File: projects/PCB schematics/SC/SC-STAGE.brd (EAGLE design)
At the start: 160 x 100 mm, 0 parts

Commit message: SC - Stage initial placement.
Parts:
- added BSPD, BSPDPLAUS1, BSPDPLAUS2, IMD: (no value), con-lstb:MA03-1
- added LED1, LED2, LED3, LED4: 150080VS75000, 150080VS75000:LEDC2012X80N
- added NOT1: 74LS19D, 74xx-us:SO14
- added Q1, Q2, Q3, Q4: IRLZ44Z, transistor-power:TO220BH
- added R1, R10, R11, R12, R2, R3, R4, R9: (no value), rcl:R0805
- added R13, R14, R5, R6: 47k, rcl:R0805
- added R15, R16, R7, R8: 100, rcl:R0805
- added U1, U2, U3, U4: G5LE-1A-E-DC12, IowaFormula:G5LE-1A-E-DC12
- added X1, X3, X4, X5, X6: 5566-2, con-molex:5566-2
- added X2: 5566-4, con-molex:5566-4
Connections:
- new net +12V: U1.5, U2.5, U3.5, U4.5
- new net +12V-ISO: X1.1, X1.2
- new net BSPDFAULT_LED: BSPD.1, X2.1
- new net BSPDPLAUS1_LED: BSPDPLAUS1.1, X2.2
- new net BSPDPLAUS2_LED: BSPDPLAUS2.1, X2.3
- new net GND: BSPD.3, BSPDPLAUS1.3, BSPDPLAUS2.3, IMD.3, NOT1.7, Q1.S, Q2.S, Q3.S, Q4.S, R11.1, R12.1, R13.1, R14.1, R3.1, R4.1, R5.1, R6.1, X5.1, X5.2
- new net IMDFAULT_LED: IMD.1, X2.4
- new net LED4: LED4.1, R11.2
- new net N$1: Q1.G, R7.2
- new net N$10: U3.1, U4.3
- new net N$105105: BSPD.2, NOT1.13, R1.1
- new net N$11552: BSPDPLAUS1.2, NOT1.11, R2.1
- new net N$14: Q4.G, R15.2
- new net N$15: LED4.2, NOT1.2, R13.2, R15.1
- new net N$17: Q4.D, U4.2
- new net N$18: Q3.G, R16.2
- new net N$19: LED3.2, NOT1.8, R14.2, R16.1
- new net N$2: LED1.2, NOT1.12, R5.2, R7.1
- new net N$20: LED3.1, R12.2
- new net N$21: Q3.D, U3.2
- new net N$3: LED1.1, R3.2
- new net N$38: U2.1, U3.3
- new net N$4: Q1.D, U1.2
- new net N$5: Q2.G, R8.2
- new net N$6: LED2.2, NOT1.10, R6.2, R8.1
- new net N$626: BSPDPLAUS2.2, NOT1.9, R10.1
- new net N$7: LED2.1, R4.2
- new net N$8: Q2.D, U2.2
- new net N$9: U1.1, U2.3
- new net N$9581: IMD.2, NOT1.1, R9.1
- new net SC+: U1.3, X4.1, X4.2
- new net SC-: U4.1, X6.1, X6.2
- new net VCC: NOT1.14, R1.2, R10.2, R2.2, R9.2, X3.1, X3.2
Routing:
- net VCC: track 0.00 -> 93.8 mm, vias 0 -> 5
- net BSPDFAULT_LED: track 0.00 -> 59.4 mm
- net BSPDPLAUS1_LED: track 0.00 -> 38.7 mm
- net BSPDPLAUS2_LED: track 0.00 -> 37.0 mm
- net IMDFAULT_LED: track 0.00 -> 18.1 mm
- net N$105105: track 0.00 -> 18.1 mm
- net N$626: track 0.00 -> 3.94 mm
- net N$11552: track 0.00 -> 3.94 mm
- net N$9581: track 0.00 -> 3.94 mm
- added copper zone on layer 1, net GND
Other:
- board size 160 x 100 mm -> 99.1 x 99.1 mm

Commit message: SC - SC-STAGE Rev. A
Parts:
- moved BSPDPLAUS1 1.27 mm to (53.3, 73.7)
- moved Q1 1.27 mm to (14.0, 55.9)
- moved Q2 1.27 mm to (38.1, 55.9)
- moved Q3 1.27 mm to (61.0, 55.9)
- moved Q4 1.27 mm to (86.4, 55.9)
- moved R2 1.27 mm to (49.5, 74.9)
- renumbered X1 to 12V-ISO, X3 to VCC, X4 to SC+, X5 to GND, X6 to SC-
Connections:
- removed net +12V: U1.5, U2.5, U3.5, U4.5
- net +12V-ISO: now also U1.5, U2.5, U3.5, U4.5
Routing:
- net +12V-ISO: track 0.00 -> 197.2 mm, vias 0 -> 1
- net SC-: track 0.00 -> 157.4 mm
- net N$15: track 0.00 -> 108.1 mm, vias 0 -> 2
- net SC+: track 0.00 -> 104.2 mm
- net N$9581: track 3.94 -> 71.4 mm, vias 0 -> 1
- net N$19: track 0.00 -> 61.9 mm
- net N$6: track 0.00 -> 54.8 mm
- net N$2: track 0.00 -> 53.3 mm, vias 0 -> 2
- net N$626: track 3.94 -> 51.8 mm, vias 0 -> 1
- net N$17: track 0.00 -> 37.1 mm
- net N$8: track 0.00 -> 36.7 mm
- net N$21: track 0.00 -> 36.7 mm
- net N$4: track 0.00 -> 36.6 mm
- net N$11552: track 3.94 -> 37.2 mm, vias 0 -> 1
- net N$14: track 0.00 -> 33.2 mm
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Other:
- board text added: "Authors: github.com/michaelpass"
- board text added: "Iowa Formula"
- board text added: "Off"
- board text added: "On"
- board text added: "Shutdown Fault Staging Board (SC-STAGE) Rev A: May 2nd, 2019"

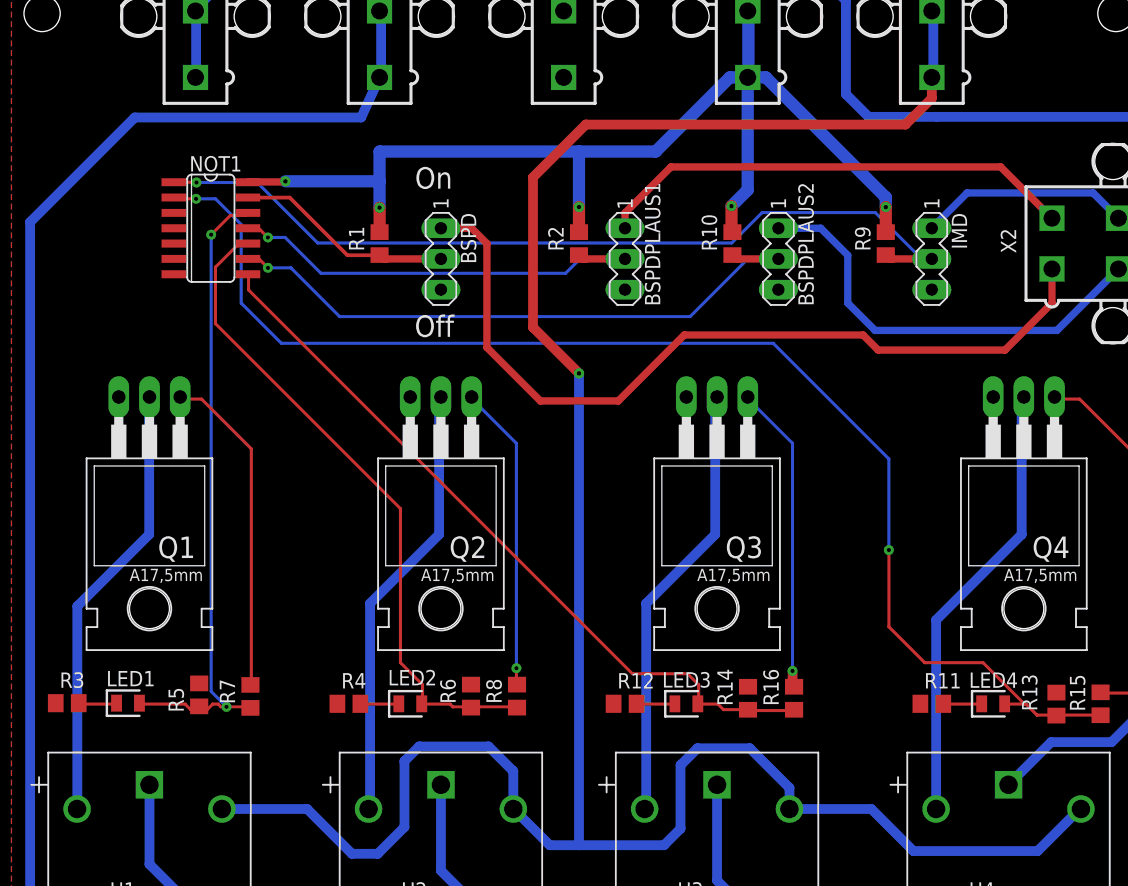
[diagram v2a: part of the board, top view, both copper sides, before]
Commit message: RTDS + TSAL Board update
Minor board & schematic errors corrected
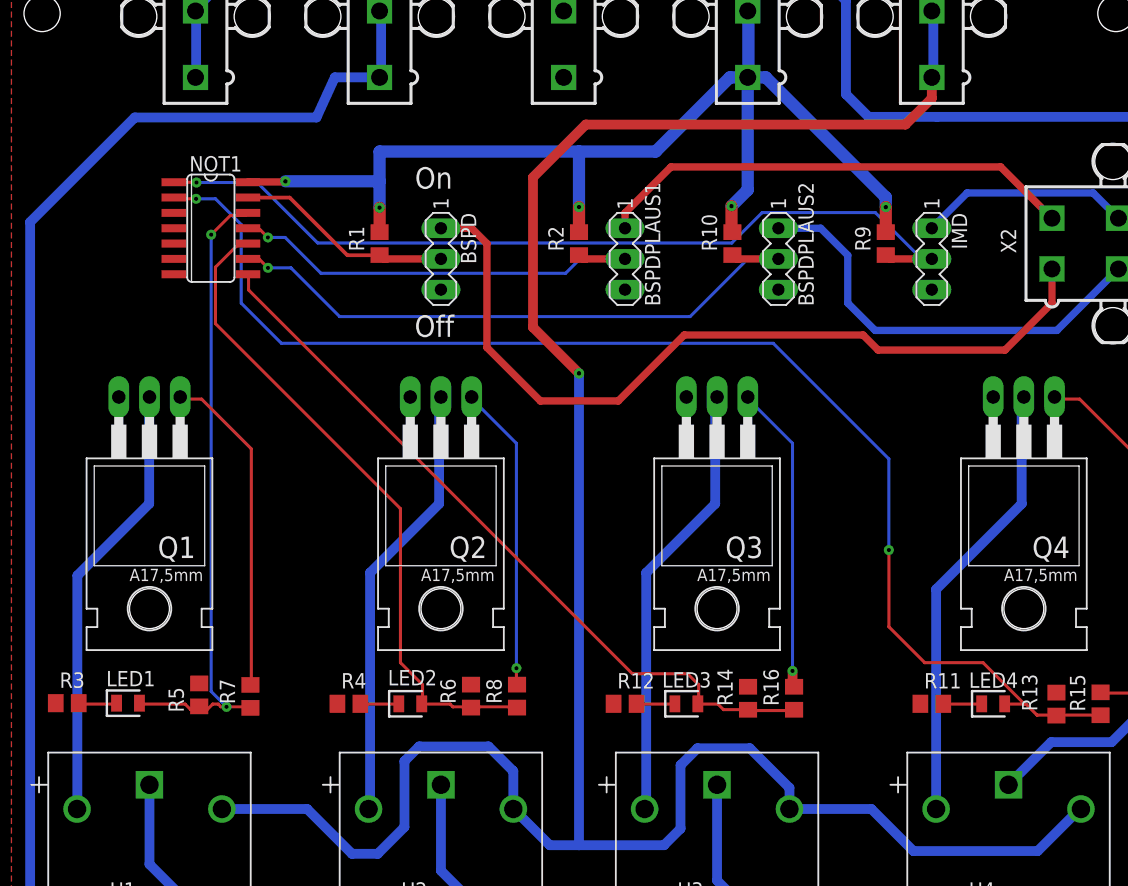
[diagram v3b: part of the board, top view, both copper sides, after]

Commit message: PROJ - Final pre-purchase revisions (4 boards still in progress.)
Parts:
- renumbered 12V-ISO to +12V-ISO.1, GND to GND.1, VCC to VCC.1, X2 to INPUT
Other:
- board text added: "INPUT: 1. BSPDFAULT_LED 2. BSPDPLAUS1_LED 3. BSPDPLAUS2_LED 4. IMDFAULT_LED"
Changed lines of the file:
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@@
 Rev A: May 2nd, 2019</text>
 <text x="63.8048" y="2.2606" size="1.016" layer="25" font="vector">Authors: github.com/michaelpass</text>
+<text x="68.58" y="60.96" size="0.8128" layer="21">INPUT:
+1. BSPDFAULT_LED
+2. BSPDPLAUS1_LED
+3. BSPDPLAUS2_LED
+4. IMDFAULT_LED</text>
 </plain>
 <attributes>
@@
 </autorouter>
 <elements>
-<element name="12V-ISO" library="con-molex" library_urn="urn:adsk.eagle:library:165" package="5566-2" package3d_urn="urn:adsk.eagle:package:8078583/1" value="5566-2" x="78.74" y="91.44" smashed="yes">
+<element name="+12V-ISO.1" library="con-molex" library_urn="urn:adsk.eagle:library:165" package="5566-2" package3d_urn="urn:adsk.eagle:package:8078583/1" value="5566-2" x="78.74" y="91.44" smashed="yes">
 <attribute name="MF" value="MOLEX" x="78.74" y="91.44" size="1.778" layer="27" display="off"/>
 <attribute name="MPN" value="" x="78.74" y="91.44" size="1.778" layer="27" display="off"/>
-<attribute name="NAME" x="77.47" y="96.52" size="1.27" layer="25"/>
+<attribute name="NAME" x="73.66" y="96.52" size="1.27" layer="25"/>
 <attribute name="OC_FARNELL" value="1822072" x="78.74" y="91.44" size="1.778" layer="27" display="off"/>
 <attribute name="OC_NEWARK" value="unknown" x="78.74" y="91.44" size="1.778" layer="27" display="off"/>
 <attribute name="VALUE" x="76.2" y="85.09" size="1.27" layer="27"/>
 </element>
-<element name="VCC" library="con-molex" library_urn="urn:adsk.eagle:library:165" package="5566-2" package3d_urn="urn:adsk.eagle:package:8078583/1" value="5566-2" x="63.5" y="91.44" smashed="yes">
+<element name="VCC.1" library="con-molex" library_urn="urn:adsk.eagle:library:165" package="5566-2" package3d_urn="urn:adsk.eagle:package:8078583/1" value="5566-2" x="63.5" y="91.44" smashed="yes">
 <attribute name="MF" value="MOLEX" x="63.5" y="91.44" size="1.778" layer="27" display="off"/>
 <attribute name="MPN" value="" x="63.5" y="91.44" size="1.778" layer="27" display="off"/>
-<attribute name="NAME" x="62.23" y="96.52" size="1.27" layer="25"/>
+<attribute name="NAME" x="60.96" y="96.52" size="1.27" layer="25"/>
 <attribute name="OC_FARNELL" value="1822072" x="63.5" y="91.44" size="1.778" layer="27" display="off"/>
 <attribute name="OC_NEWARK" value="unknown" x="63.5" y="91.44" size="1.778" layer="27" display="off"/>
 <attribute name="VALUE" x="60.96" y="85.09" size="1.27" layer="27"/>
 </element>
-<element name="GND" library="con-molex" library_urn="urn:adsk.eagle:library:165" package="5566-2" package3d_urn="urn:adsk.eagle:package:8078583/1" value="5566-2" x="48.26" y="91.44" smashed="yes">
+<element name="GND.1" library="con-molex" library_urn="urn:adsk.eagle:library:165" package="5566-2" package3d_urn="urn:adsk.eagle:package:8078583/1" value="5566-2" x="48.26" y="91.44" smashed="yes">
 <attribute name="MF" value="MOLEX" x="48.26" y="91.44" size="1.778" layer="27" display="off"/>
 <attribute name="MPN" value="" x="48.26" y="91.44" size="1.778" layer="27" display="off"/>
-<attribute name="NAME" x="46.99" y="96.52" size="1.27" layer="25"/>
+<attribute name="NAME" x="45.72" y="96.52" size="1.27" layer="25"/>
 <attribute name="OC_FARNELL" value="1822072" x="48.26" y="91.44" size="1.778" layer="27" display="off"/>
 <attribute name="OC_NEWARK" value="unknown" x="48.26" y="91.44" size="1.778" layer="27" display="off"/>
@@
 <attribute name="VENDOR" value="OMRON" x="13.97" y="1.27" size="1.778" layer="27" display="off"/>
 </element>
-<element name="X2" library="con-molex" library_urn="urn:adsk.eagle:library:165" package="5566-4" package3d_urn="urn:adsk.eagle:package:8078582/1" value="5566-4" x="91.44" y="74.93" smashed="yes" rot="R270">
+<element name="INPUT" library="con-molex" library_urn="urn:adsk.eagle:library:165" package="5566-4" package3d_urn="urn:adsk.eagle:package:8078582/1" value="5566-4" x="91.44" y="74.93" smashed="yes" rot="R270">
 <attribute name="MF" value="MOLEX" x="91.44" y="74.93" size="1.778" layer="27" rot="R270" display="off"/>
 <attribute name="MPN" value="" x="91.44" y="74.93" size="1.778" layer="27" rot="R270" display="off"/>
@@
 <signals>
 <signal name="GND">
-<contactref element="GND" pad="1"/>
-<contactref element="GND" pad="2"/>
+<contactref element="GND.1" pad="1"/>
+<contactref element="GND.1" pad="2"/>
 <contactref element="Q1" pad="S"/>
 <contactref element="R5" pad="1"/>
@@
 </signal>
 <signal name="VCC">
-<contactref element="VCC" pad="1"/>
-<contactref element="VCC" pad="2"/>
+<contactref element="VCC.1" pad="1"/>
+<contactref element="VCC.1" pad="2"/>
 <contactref element="R1" pad="2"/>
 <contactref element="R2" pad="2"/>
@@
 </signal>
 <signal name="+12V-ISO">
-<contactref element="12V-ISO" pad="1"/>
-<contactref element="12V-ISO" pad="2"/>
+<contactref element="+12V-ISO.1" pad="1"/>
+<contactref element="+12V-ISO.1" pad="2"/>
 <wire x1="78.867" y1="94.1832" x2="78.867" y2="88.6968" width="0.8128" layer="16"/>
 <wire x1="78.867" y1="88.6968" x2="78.74" y2="88.69" width="0.254" layer="16"/>
@@
 </signal>
 <signal name="BSPDFAULT_LED">
-<contactref element="X2" pad="1"/>
+<contactref element="INPUT" pad="1"/>
 <contactref element="BSPD" pad="1"/>
 <wire x1="88.69" y1="72.83" x2="88.69" y2="72.39" width="0.6096" layer="1"/>
@@
 </signal>
 <signal name="BSPDPLAUS1_LED">
-<contactref element="X2" pad="2"/>
+<contactref element="INPUT" pad="2"/>
 <contactref element="BSPDPLAUS1" pad="1"/>
 <wire x1="88.69" y1="77.03" x2="84.44" y2="81.28" width="0.6096" layer="1"/>
@@
 </signal>
 <signal name="BSPDPLAUS2_LED">
-<contactref element="X2" pad="3"/>
+<contactref element="INPUT" pad="3"/>
 <contactref element="BSPDPLAUS2" pad="1"/>
 <wire x1="94.19" y1="72.83" x2="89.1018" y2="67.7418" width="0.6096" layer="16"/>
@@
 </signal>
 <signal name="IMDFAULT_LED">
-<contactref element="X2" pad="4"/>
+<contactref element="INPUT" pad="4"/>
 <contactref element="IMD" pad="1"/>
 <wire x1="78.74" y1="76.2" x2="81.661" y2="79.121" width="0.6096" layer="16"/>

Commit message: PROJ - Gerber files major milestone - 05/05/19.
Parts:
- R1, R10, R2, R9: value (none) -> 10k
- R11, R12, R3, R4: value (none) -> 82
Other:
- board text added: "Shutdown Fault Staging Board (SC-STAGE) Rev A: May 5th, 2019"
- board text removed: "Shutdown Fault Staging Board (SC-STAGE) Rev A: May 2nd, 2019"
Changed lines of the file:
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@@
 <text x="16.6116" y="3.4544" size="1.778" layer="25" font="vector">Iowa Formula</text>
 <text x="42.0624" y="3.0734" size="1.397" layer="25">Shutdown Fault Staging Board (SC-STAGE)
-Rev A: May 2nd, 2019</text>
+Rev A: May 5th, 2019</text>
 <text x="63.8048" y="2.2606" size="1.016" layer="25" font="vector">Authors: github.com/michaelpass</text>
 <text x="68.58" y="60.96" size="0.8128" layer="21">INPUT:
@@
 <attribute name="VALUE" x="17.907" y="53.34" size="1.778" layer="27" ratio="10" rot="R180"/>
 </element>
-<element name="R1" library="rcl" library_urn="urn:adsk.eagle:library:334" package="R0805" package3d_urn="urn:adsk.eagle:package:23553/2" value="" x="33.02" y="74.93" smashed="yes" rot="R90">
+<element name="R1" library="rcl" library_urn="urn:adsk.eagle:library:334" package="R0805" package3d_urn="urn:adsk.eagle:package:23553/2" value="10k" x="33.02" y="74.93" smashed="yes" rot="R90">
 <attribute name="NAME" x="31.75" y="74.295" size="1.27" layer="25" rot="R90"/>
 <attribute name="SPICEPREFIX" value="R" x="33.02" y="74.93" size="1.778" layer="27" rot="R90" display="off"/>
@@
 <attribute name="NAME" x="12.4206" y="38.9128" size="1.27" layer="25" rot="R180" align="center"/>
 </element>
-<element name="R3" library="rcl" library_urn="urn:adsk.eagle:library:334" package="R0805" package3d_urn="urn:adsk.eagle:package:23553/2" value="" x="7.1628" y="36.8808" smashed="yes">
+<element name="R3" library="rcl" library_urn="urn:adsk.eagle:library:334" package="R0805" package3d_urn="urn:adsk.eagle:package:23553/2" value="82" x="7.1628" y="36.8808" smashed="yes">
 <attribute name="NAME" x="6.5278" y="38.1508" size="1.27" layer="25"/>
 <attribute name="SPICEPREFIX" value="R" x="7.1628" y="36.8808" size="1.778" layer="27" display="off"/>
@@
 <attribute name="VALUE" x="42.037" y="53.34" size="1.778" layer="27" ratio="10" rot="R180"/>
 </element>
-<element name="R2" library="rcl" library_urn="urn:adsk.eagle:library:334" package="R0805" package3d_urn="urn:adsk.eagle:package:23553/2" value="" x="49.53" y="74.93" smashed="yes" rot="R90">
+<element name="R2" library="rcl" library_urn="urn:adsk.eagle:library:334" package="R0805" package3d_urn="urn:adsk.eagle:package:23553/2" value="10k" x="49.53" y="74.93" smashed="yes" rot="R90">
 <attribute name="NAME" x="48.26" y="74.295" size="1.27" layer="25" rot="R90"/>
 <attribute name="SPICEPREFIX" value="R" x="39.37" y="40.64" size="1.778" layer="27" rot="R90" display="off"/>
@@
 <attribute name="NAME" x="35.7378" y="38.989" size="1.27" layer="25" align="center"/>
 </element>
-<element name="R4" library="rcl" library_urn="urn:adsk.eagle:library:334" package="R0805" package3d_urn="urn:adsk.eagle:package:23553/2" value="" x="30.48" y="36.83" smashed="yes">
+<element name="R4" library="rcl" library_urn="urn:adsk.eagle:library:334" package="R0805" package3d_urn="urn:adsk.eagle:package:23553/2" value="82" x="30.48" y="36.83" smashed="yes">
 <attribute name="NAME" x="29.845" y="38.1" size="1.27" layer="25"/>
 <attribute name="SPICEPREFIX" value="R" x="15.24" y="38.1" size="1.778" layer="27" display="off"/>
@@
 <attribute name="VALUE" x="90.297" y="53.34" size="1.778" layer="27" ratio="10" rot="R180"/>
 </element>
-<element name="R9" library="rcl" library_urn="urn:adsk.eagle:library:334" package="R0805" package3d_urn="urn:adsk.eagle:package:23553/2" value="" x="74.93" y="74.93" smashed="yes" rot="R90">
+<element name="R9" library="rcl" library_urn="urn:adsk.eagle:library:334" package="R0805" package3d_urn="urn:adsk.eagle:package:23553/2" value="10k" x="74.93" y="74.93" smashed="yes" rot="R90">
 <attribute name="NAME" x="73.66" y="74.295" size="1.27" layer="25" rot="R90"/>
 <attribute name="SPICEPREFIX" value="R" x="64.77" y="38.1" size="1.778" layer="27" rot="R90" display="off"/>
@@
 <attribute name="NAME" x="83.8454" y="38.7858" size="1.27" layer="25" align="center"/>
 </element>
-<element name="R11" library="rcl" library_urn="urn:adsk.eagle:library:334" package="R0805" package3d_urn="urn:adsk.eagle:package:23553/2" value="" x="78.74" y="36.83" smashed="yes">
+<element name="R11" library="rcl" library_urn="urn:adsk.eagle:library:334" package="R0805" package3d_urn="urn:adsk.eagle:package:23553/2" value="82" x="78.74" y="36.83" smashed="yes">
 <attribute name="NAME" x="78.105" y="38.1" size="1.27" layer="25"/>
 <attribute name="SPICEPREFIX" value="R" x="63.5" y="38.1" size="1.778" layer="27" display="off"/>
@@
 <attribute name="VALUE" x="64.897" y="53.34" size="1.778" layer="27" ratio="10" rot="R180"/>
 </element>
-<element name="R10" library="rcl" library_urn="urn:adsk.eagle:library:334" package="R0805" package3d_urn="urn:adsk.eagle:package:23553/2" value="" x="62.23" y="74.93" smashed="yes" rot="R90">
+<element name="R10" library="rcl" library_urn="urn:adsk.eagle:library:334" package="R0805" package3d_urn="urn:adsk.eagle:package:23553/2" value="10k" x="62.23" y="74.93" smashed="yes" rot="R90">
 <attribute name="NAME" x="60.96" y="74.295" size="1.27" layer="25" rot="R90"/>
 <attribute name="SPICEPREFIX" value="R" x="52.07" y="38.1" size="1.778" layer="27" rot="R90" display="off"/>
@@
 <attribute name="NAME" x="58.4454" y="38.8112" size="1.27" layer="25" align="center"/>
 </element>
-<element name="R12" library="rcl" library_urn="urn:adsk.eagle:library:334" package="R0805" package3d_urn="urn:adsk.eagle:package:23553/2" value="" x="53.34" y="36.83" smashed="yes">
+<element name="R12" library="rcl" library_urn="urn:adsk.eagle:library:334" package="R0805" package3d_urn="urn:adsk.eagle:package:23553/2" value="82" x="53.34" y="36.83" smashed="yes">
 <attribute name="NAME" x="52.705" y="38.1" size="1.27" layer="25"/>
 <attribute name="SPICEPREFIX" value="R" x="38.1" y="38.1" size="1.778" layer="27" display="off"/>
@@
 <wire x1="36.2966" y1="33.2994" x2="35.0774" y2="32.0802" width="0.8128" layer="16"/>
 <wire x1="42.037" y1="33.2994" x2="36.2966" y2="33.2994" width="0.8128" layer="16"/>
-<wire x1="42.037" y1="33.2994" x2="44.0182" y2="31.3182" width="0.8128" layer="16"/>
+<wire x1="42.037" y1="33.2994" x2="44.0944" y2="31.242" width="0.8128" layer="16"/>
 <contactref element="U3" pad="5"/>
 <wire x1="66.9544" y1="28.1178" x2="66.9544" y2="29.8704" width="0.8128" layer="16"/>
@@
 <wire x1="57.9374" y1="26.4922" x2="57.9374" y2="31.75" width="0.8128" layer="16"/>
 <wire x1="56.5658" y1="25.1206" x2="57.9374" y2="26.4922" width="0.8128" layer="16"/>
-<wire x1="47.117" y1="25.1206" x2="49.53" y2="25.1206" width="0.8128" layer="16"/>
 <wire x1="49.53" y1="25.1206" x2="56.5658" y2="25.1206" width="0.8128" layer="16"/>
-<wire x1="44.1198" y1="28.1178" x2="47.117" y2="25.1206" width="0.8128" layer="16"/>
 <contactref element="U4" pad="5"/>
 <wire x1="73.7362" y1="28.1178" x2="77.216" y2="24.638" width="0.8128" layer="16"/>
@@
 <wire x1="90.9828" y1="28.1178" x2="87.503" y2="24.638" width="0.8128" layer="16"/>
 <wire x1="90.9828" y1="28.1178" x2="91.0844" y2="28.1178" width="0.254" layer="16"/>
-<wire x1="44.0182" y1="31.3182" x2="44.0944" y2="31.242" width="0.8128" layer="16"/>
 <wire x1="44.0944" y1="31.242" x2="44.0944" y2="28.1178" width="0.8128" layer="16"/>
 <wire x1="66.9544" y1="28.1178" x2="73.7362" y2="28.1178" width="0.8128" layer="16"/>
@@
 <wire x1="78.74" y1="86.9628" x2="78.74" y2="88.69" width="0.8128" layer="1"/>
 <wire x1="50.0888" y1="84.7852" x2="76.5624" y2="84.7852" width="0.8128" layer="1"/>
-<wire x1="44.0944" y1="28.1178" x2="44.1198" y2="28.1178" width="0" layer="19" extent="16-16"/>
+<wire x1="44.0944" y1="28.1178" x2="47.0916" y2="25.1206" width="0.8128" layer="16"/>
+<wire x1="47.0916" y1="25.1206" x2="49.53" y2="25.1206" width="0.8128" layer="16"/>
 </signal>
 <signal name="N$1">
